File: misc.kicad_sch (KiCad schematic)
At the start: 35 parts

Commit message: [#54084] Sheets cleanup
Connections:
- net VDDI4 is gone; now on net VDDI: C?.1, C?.1, C?.1, C?.1, C?.1, C?.1, R?.2, R?.2, R?.2, R?.2, R?.2, R?.2, R?.2, R?.2, R?.2, R?.2, U?.C6 (VCCQ), U?.M4 (VCCQ), U?.N4 (VCCQ), U?.P3 (VCCQ), U?.P5 (VCCQ)
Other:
- note added: "PolarFire Bank 3 JTAG/DEDIO"
- note added: "PolarFire Bank 4 MSSIO"
- company: (none) -> Antmicro Ltd
- title: (none) -> PolarFire SoM
- moved on the sheet: C?, J?, R?, U?, U?D, U?E

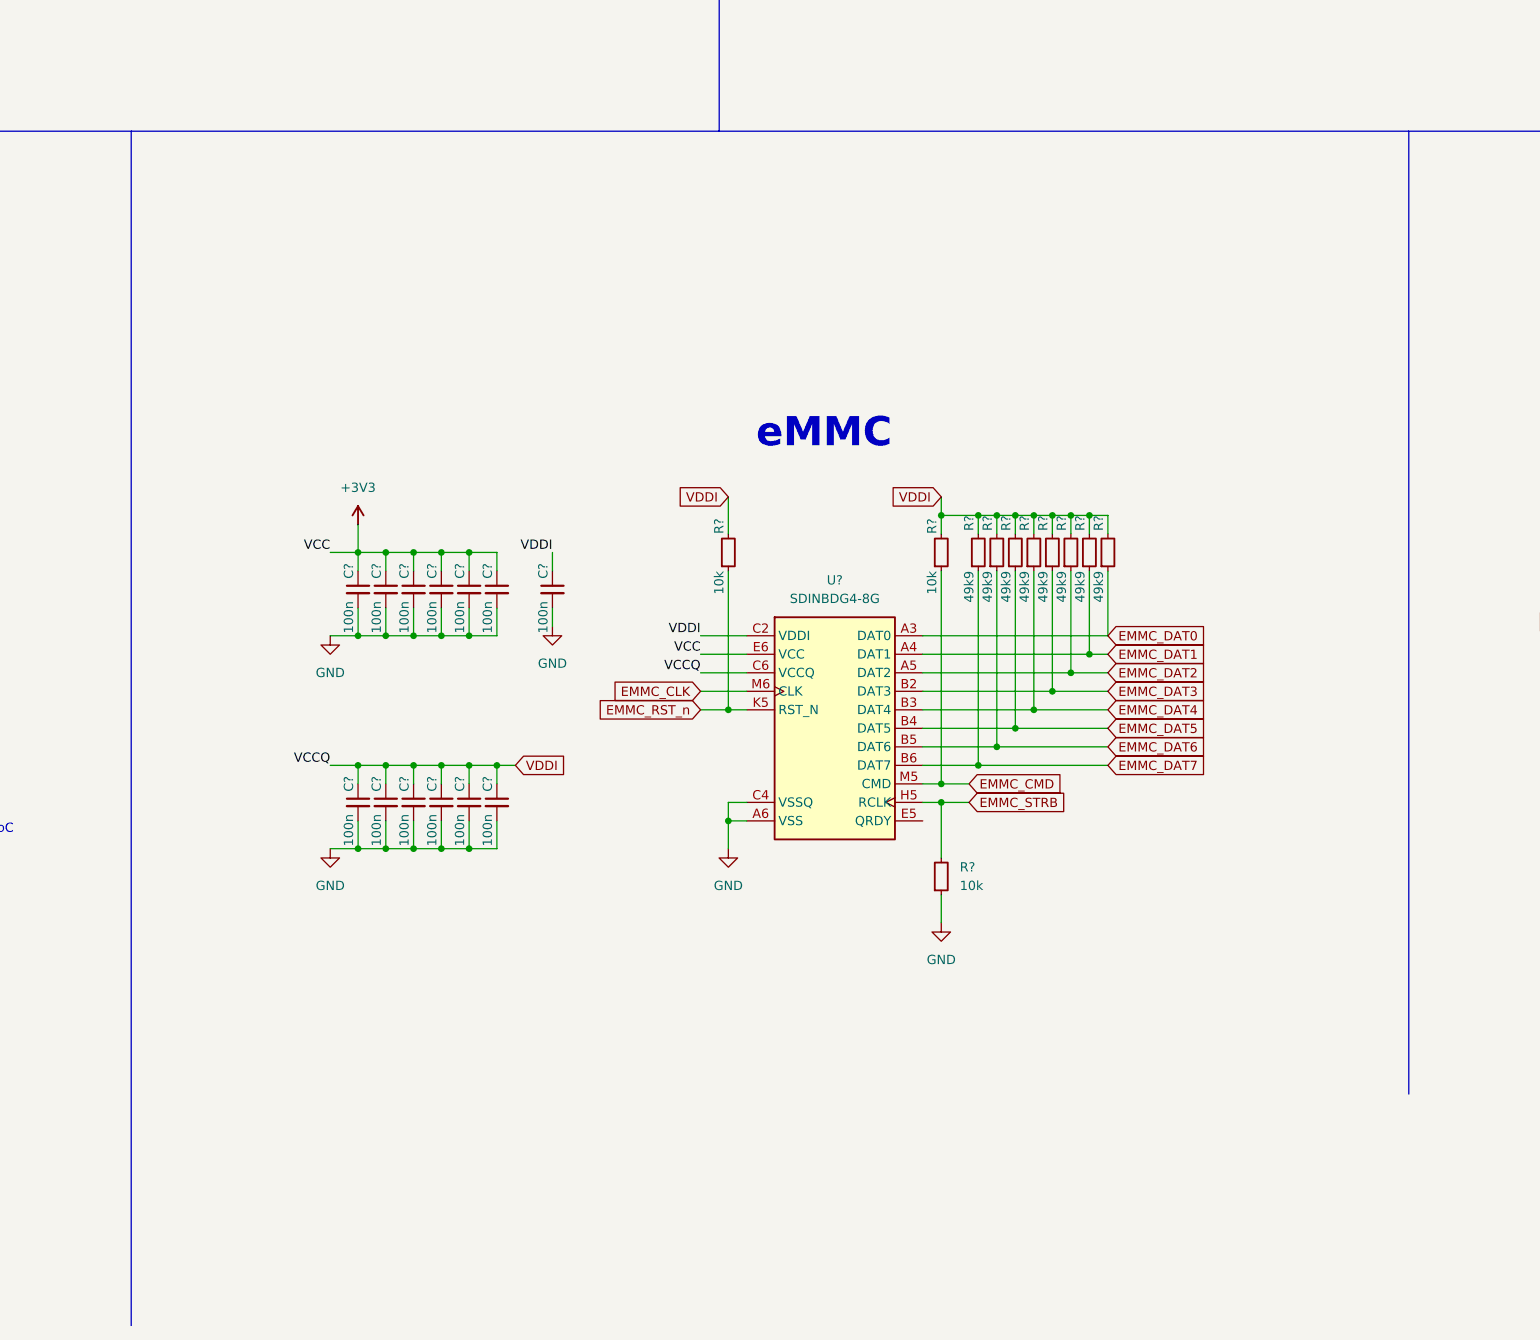
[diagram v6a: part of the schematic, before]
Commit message: [#54016] Relabel eMMC supply nets
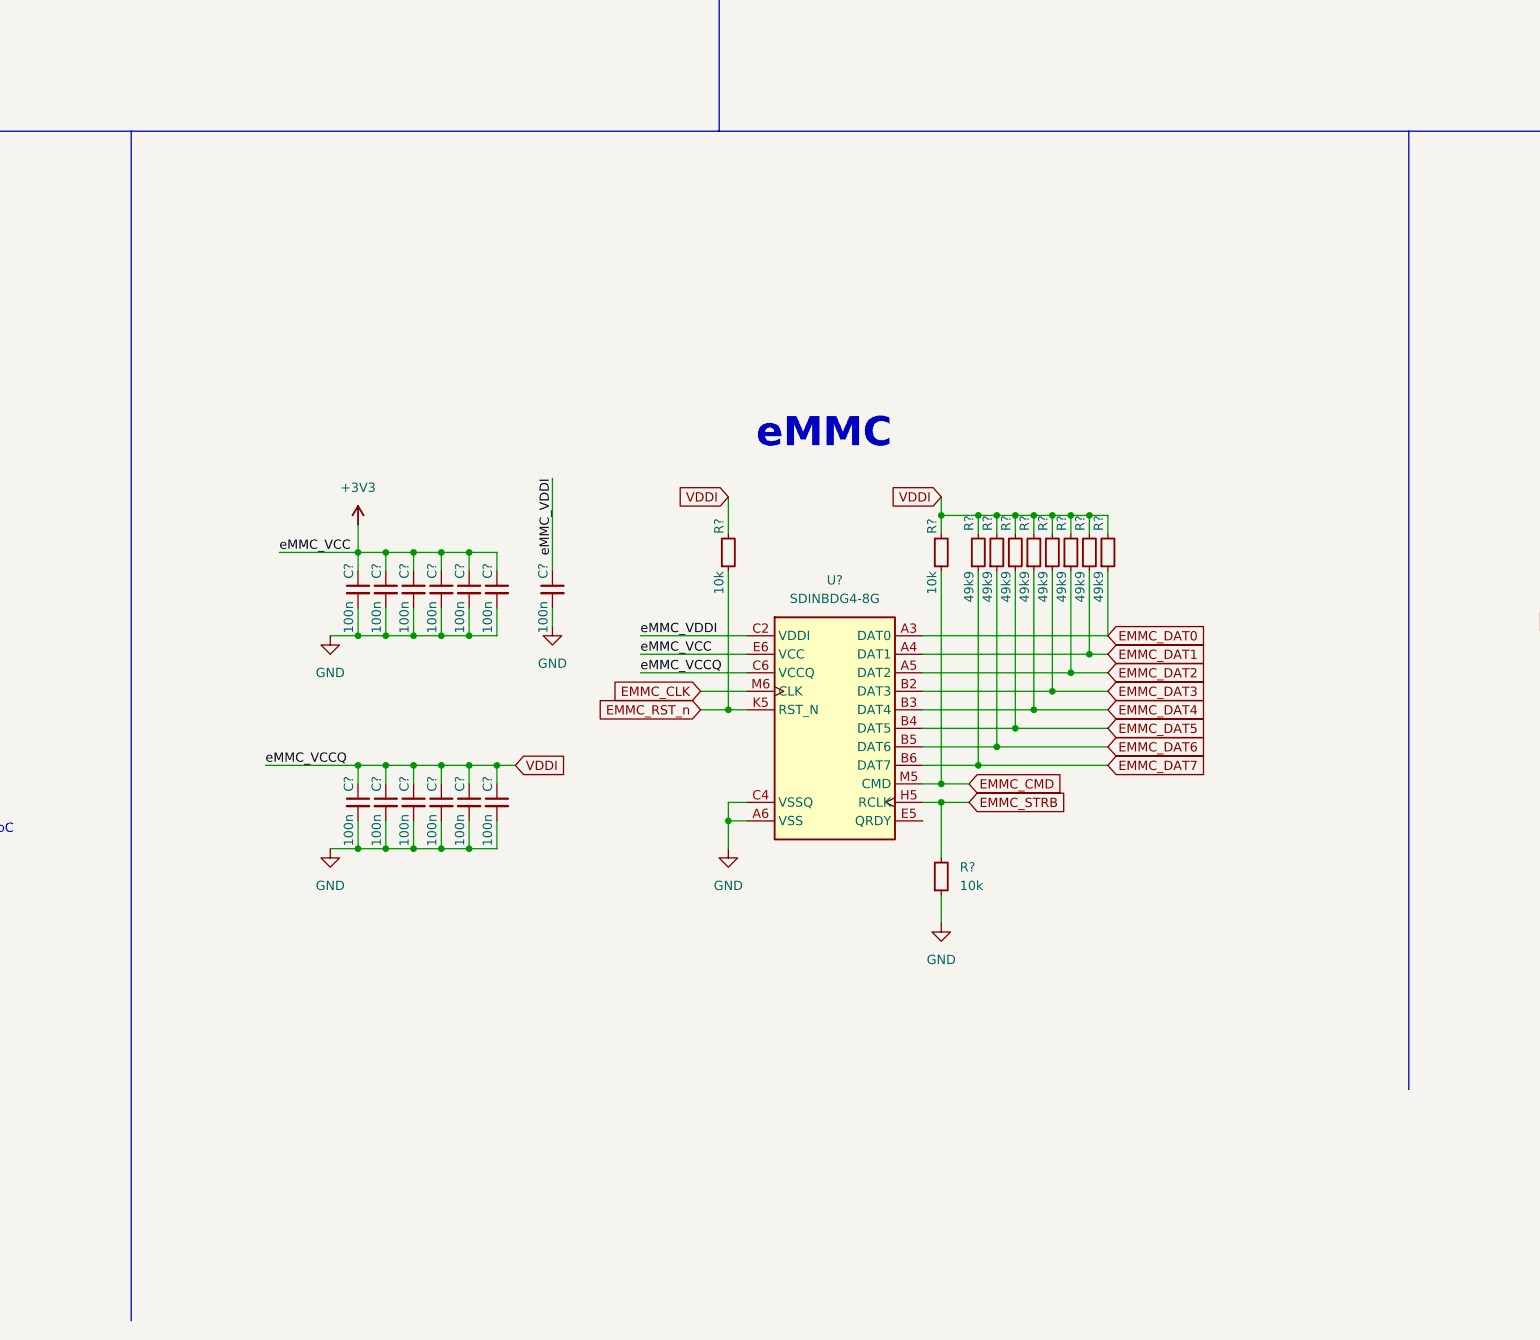
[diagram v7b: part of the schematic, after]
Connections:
- net VDDI: no longer C?.1, U?.C2 (VDDI)
- new net eMMC_VDDI: C?.1, U?.C2 (VDDI)
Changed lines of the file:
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@@
     (stroke (width 0) (type default) (color 0 0 0 0))
   )
-  (wire (pts (xy 165.1 179.07) (xy 168.91 179.07))
+  (wire (pts (xy 158.115 179.07) (xy 168.91 179.07))
     (stroke (width 0) (type default) (color 0 0 0 0))
   )
@@
     (stroke (width 0) (type default) (color 0 0 0 0))
   )
-  (polyline (pts (xy 137.795 285.115) (xy 137.795 121.285))
+  (polyline (pts (xy 137.795 284.48) (xy 137.795 121.285))
     (stroke (width 0) (type default) (color 0 0 0 0))
   )
@@
     (stroke (width 0) (type default) (color 0 0 0 0))
   )
-  (wire (pts (xy 165.1 208.28) (xy 168.91 208.28))
+  (wire (pts (xy 156.21 208.28) (xy 168.91 208.28))
     (stroke (width 0) (type default) (color 0 0 0 0))
   )
@@
     (stroke (width 0) (type default) (color 0 0 0 0))
   )
-  (wire (pts (xy 195.58 179.07) (xy 195.58 181.61))
+  (wire (pts (xy 195.58 168.91) (xy 195.58 181.61))
     (stroke (width 0) (type default) (color 0 0 0 0))
   )
@@
     (stroke (width 0) (type default) (color 0 0 0 0))
   )
-  (wire (pts (xy 215.9 195.58) (xy 222.25 195.58))
+  (wire (pts (xy 207.645 195.58) (xy 222.25 195.58))
     (stroke (width 0) (type default) (color 0 0 0 0))
   )
@@
     (stroke (width 0) (type default) (color 0 0 0 0))
   )
-  (wire (pts (xy 215.9 193.04) (xy 222.25 193.04))
+  (wire (pts (xy 207.645 193.04) (xy 222.25 193.04))
     (stroke (width 0) (type default) (color 0 0 0 0))
   )
@@
     (stroke (width 0) (type default) (color 0 0 0 0))
   )
-  (wire (pts (xy 215.9 190.5) (xy 222.25 190.5))
+  (wire (pts (xy 207.645 190.5) (xy 222.25 190.5))
     (stroke (width 0) (type default) (color 0 0 0 0))
   )
@@
     (stroke (width 0) (type default) (color 0 0 0 0))
   )
-  (polyline (pts (xy 313.055 253.365) (xy 313.055 121.285))
+  (polyline (pts (xy 313.055 252.73) (xy 313.055 121.285))
     (stroke (width 0) (type default) (color 0 0 0 0))
   )
@@
     (effects (font (size 4 4) (thickness 0.8) bold) (justify left bottom))
   )
-  (label "VCCQ" (at 215.9 195.58 180)
+  (label "eMMC_VCCQ" (at 207.645 195.58 0)
+    (effects (font (size 1.27 1.27)) (justify left bottom))
+  )
+  (label "eMMC_VCC" (at 158.115 179.07 0)
+    (effects (font (size 1.27 1.27)) (justify left bottom))
+  )
+  (label "eMMC_VCCQ" (at 156.21 208.28 0)
+    (effects (font (size 1.27 1.27)) (justify left bottom))
+  )
+  (label "eMMC_VCC" (at 207.645 193.04 0)
+    (effects (font (size 1.27 1.27)) (justify left bottom))
+  )
+  (label "eMMC_VDDI" (at 195.58 168.91 270)
     (effects (font (size 1.27 1.27)) (justify right bottom))
   )
-  (label "VCC" (at 165.1 179.07 180)
-    (effects (font (size 1.27 1.27)) (justify right bottom))
-  )
-  (label "VCCQ" (at 165.1 208.28 180)
-    (effects (font (size 1.27 1.27)) (justify right bottom))
-  )
-  (label "VCC" (at 215.9 193.04 180)
-    (effects (font (size 1.27 1.27)) (justify right bottom))
-  )
-  (label "VDDI" (at 195.58 179.07 180)
-    (effects (font (size 1.27 1.27)) (justify right bottom))
-  )
-  (label "VDDI" (at 215.9 190.5 180)
-    (effects (font (size 1.27 1.27)) (justify right bottom))
+  (label "eMMC_VDDI" (at 207.645 190.5 0)
+    (effects (font (size 1.27 1.27)) (justify left bottom))
   )
   (global_label "MEM_DAT4" (shape input) (at 85.725 77.47 0) (fields_autoplaced)

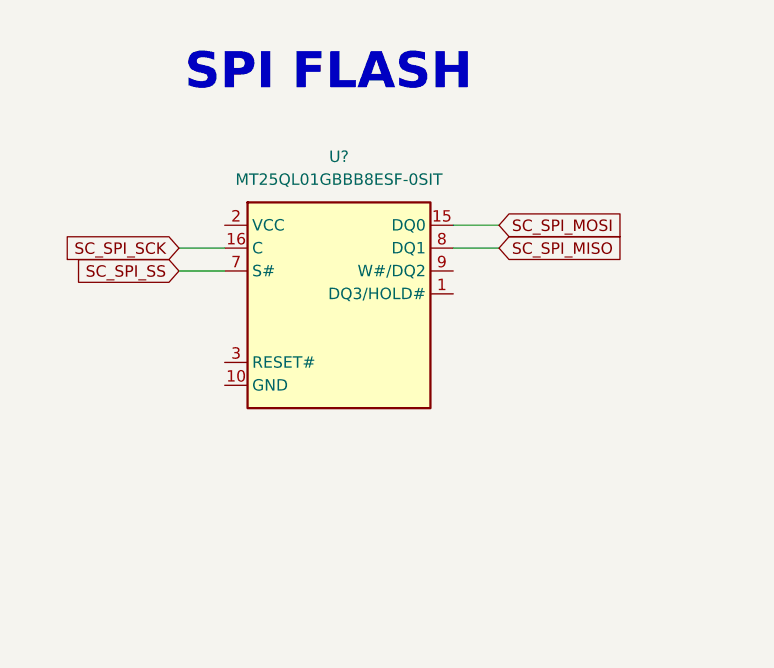
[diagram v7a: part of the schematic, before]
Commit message: [#54016] Connect power to SPI FLASH
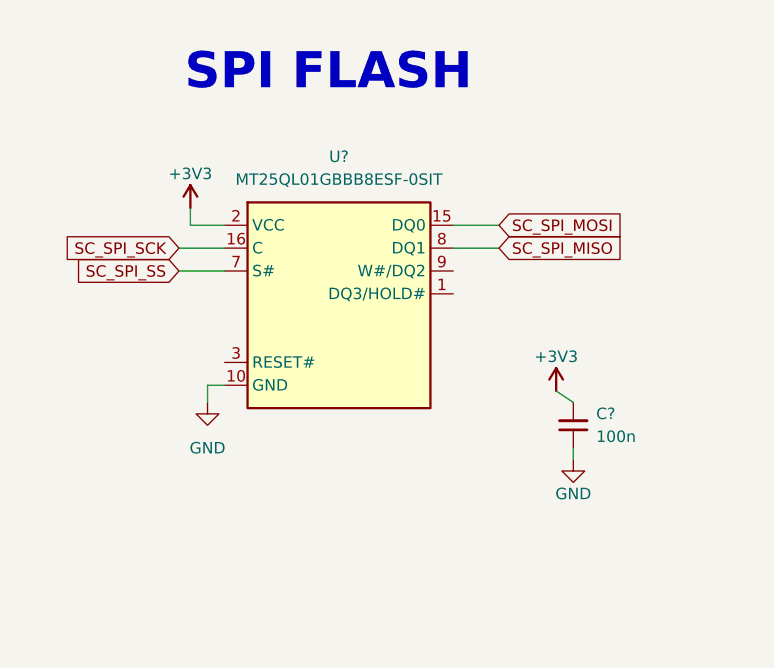
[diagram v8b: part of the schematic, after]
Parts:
- added C?: C_100n_0402, antmicro-footprints:C_0402_1005Metric, symbol antmicroCapacitors0402:C_100n_0402
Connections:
- net +3V3: now also U?.2 (VCC), C?.2
- net GND: now also U?.10 (GND), C?.1
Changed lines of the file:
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@@
     (stroke (width 0) (type default) (color 0 0 0 0))
   )
+  (wire (pts (xy 385.445 204.47) (xy 387.35 205.74))
+    (stroke (width 0) (type default) (color 0 0 0 0))
+  )
   (wire (pts (xy 184.15 215.9) (xy 184.15 219.71))
     (stroke (width 0) (type default) (color 0 0 0 0))
@@
     (stroke (width 0) (type default) (color 0 0 0 0))
   )
+  (wire (pts (xy 348.615 203.835) (xy 346.71 203.835))
+    (stroke (width 0) (type default) (color 0 0 0 0))
+  )
   (wire (pts (xy 264.16 173.99) (xy 266.7 173.99))
     (stroke (width 0) (type default) (color 0 0 0 0))
@@
     (stroke (width 0) (type default) (color 0 0 0 0))
   )
+  (wire (pts (xy 344.805 186.055) (xy 344.805 184.15))
+    (stroke (width 0) (type default) (color 0 0 0 0))
+  )
   (wire (pts (xy 259.08 173.99) (xy 261.62 173.99))
     (stroke (width 0) (type default) (color 0 0 0 0))
@@
     (stroke (width 0) (type default) (color 0 0 0 0))
   )
+  (wire (pts (xy 348.615 186.055) (xy 344.805 186.055))
+    (stroke (width 0) (type default) (color 0 0 0 0))
+  )
   (wire (pts (xy 256.54 173.99) (xy 259.08 173.99))
     (stroke (width 0) (type default) (color 0 0 0 0))
@@
     (stroke (width 0) (type default) (color 0 0 0 0))
   )
+  (wire (pts (xy 346.71 203.835) (xy 346.71 205.74))
+    (stroke (width 0) (type default) (color 0 0 0 0))
+  )
   (wire (pts (xy 133.35 68.58) (xy 138.43 68.58))
     (stroke (width 0) (type default) (color 0 0 0 0))
@@
     (stroke (width 0) (type default) (color 0 0 0 0))
   )
+  (wire (pts (xy 387.35 210.82) (xy 387.35 212.09))
+    (stroke (width 0) (type default) (color 0 0 0 0))
+  )
   (wire (pts (xy 67.945 69.85) (xy 73.025 69.85))
     (stroke (width 0) (type default) (color 0 0 0 0))
@@
     )
   )
+  (symbol (lib_id "antmicropower:+3V3") (at 385.445 204.47 0) (unit 1)
+    (in_bom yes) (on_board yes)
+    (property "Reference" "#PWR?" (id 0) (at 400.685 207.01 0)
+      (effects (font (size 1.27 1.27) (thickness 0.15)) (justify left bottom) hide)
+    )
+    (property "Value" "+3V3" (id 1) (at 385.445 200.66 0)
+      (effects (font (size 1.27 1.27) (thickness 0.15)))
+    )
+    (property "Footprint" "" (id 2) (at 400.685 212.09 0)
+      (effects (font (size 1.27 1.27) (thickness 0.15)) (justify left bottom) hide)
+    )
+    (property "Datasheet" "" (id 3) (at 400.685 214.63 0)
+      (effects (font (size 1.27 1.27) (thickness 0.15)) (justify left bottom) hide)
+    )
+    (property "Author" "Antmicro" (id 4) (at 400.685 212.09 0)
+      (effects (font (size 1.27 1.27) (thickness 0.15)) (justify left bottom) hide)
+    )
+    (property "License" "Apache-2.0" (id 5) (at 400.685 214.63 0)
+      (effects (font (size 1.27 1.27) (thickness 0.15)) (justify left bottom) hide)
+    )
+    (pin "1")
+  )
   (symbol (lib_id "antmicroResistors0402:R_49k9_0402") (at 256.54 181.61 90) (unit 1)
     (in_bom yes) (on_board yes)
@@
     (pin "1")
   )
+  (symbol (lib_id "antmicropower:GND") (at 346.71 205.74 0) (unit 1)
+    (in_bom yes) (on_board yes) (fields_autoplaced)
+    (property "Reference" "#PWR?" (id 0) (at 355.6 208.28 0)
+      (effects (font (size 1.27 1.27) (thickness 0.15)) (justify left bottom) hide)
+    )
+    (property "Value" "GND" (id 1) (at 346.71 210.82 0)
+      (effects (font (size 1.27 1.27) (thickness 0.15)))
+    )
+    (property "Footprint" "" (id 2) (at 355.6 213.36 0)
+      (effects (font (size 1.27 1.27) (thickness 0.15)) (justify left bottom) hide)
+    )
+    (property "Datasheet" "" (id 3) (at 355.6 218.44 0)
+      (effects (font (size 1.27 1.27) (thickness 0.15)) (justify left bottom) hide)
+    )
+    (property "Author" "Antmicro" (id 4) (at 355.6 213.36 0)
+      (effects (font (size 1.27 1.27) (thickness 0.15)) (justify left bottom) hide)
+    )
+    (property "License" "Apache-2.0" (id 5) (at 355.6 215.9 0)
+      (effects (font (size 1.27 1.27) (thickness 0.15)) (justify left bottom) hide)
+    )
+    (pin "1")
+  )
   (symbol (lib_id "antmicroMemory:MT25QL01GBBB8E_SOP2-16") (at 346.075 186.055 0) (unit 1)
     (in_bom yes) (on_board yes) (fields_autoplaced)
@@
     (pin "2")
   )
+  (symbol (lib_id "antmicropower:GND") (at 387.35 212.09 0) (unit 1)
+    (in_bom yes) (on_board yes)
+    (property "Reference" "#PWR?" (id 0) (at 396.24 214.63 0)
+      (effects (font (size 1.27 1.27) (thickness 0.15)) (justify left bottom) hide)
+    )
+    (property "Value" "GND" (id 1) (at 387.35 215.9 0)
+      (effects (font (size 1.27 1.27) (thickness 0.15)))
+    )
+    (property "Footprint" "" (id 2) (at 396.24 219.71 0)
+      (effects (font (size 1.27 1.27) (thickness 0.15)) (justify left bottom) hide)
+    )
+    (property "Datasheet" "" (id 3) (at 396.24 224.79 0)
+      (effects (font (size 1.27 1.27) (thickness 0.15)) (justify left bottom) hide)
+    )
+    (property "Author" "Antmicro" (id 4) (at 396.24 219.71 0)
+      (effects (font (size 1.27 1.27) (thickness 0.15)) (justify left bottom) hide)
+    )
+    (property "License" "Apache-2.0" (id 5) (at 396.24 222.25 0)
+      (effects (font (size 1.27 1.27) (thickness 0.15)) (justify left bottom) hide)
+    )
+    (pin "1")
+  )
   (symbol (lib_id "antmicroResistors0402:R_0R_0402") (at 75.565 96.52 0) (unit 1)
     (in_bom yes) (on_board yes)
@@
     (pin "2")
   )
+  (symbol (lib_id "antmicroCapacitors0402:C_100n_0402") (at 387.35 210.82 90) (unit 1)
+    (in_bom yes) (on_board yes) (fields_autoplaced)
+    (property "Reference" "C?" (id 0) (at 389.89 207.0035 90)
+      (effects (font (size 1.27 1.27) (thickness 0.15)) (justify right))
+    )
+    (property "Value" "C_100n_0402" (id 1) (at 397.51 190.5 0)
+      (effects (font (size 1.27 1.27) (thickness 0.15)) (justify left bottom) hide)
+    )
+    (property "Footprint" "antmicro-footprints:C_0402_1005Metric" (id 2) (at 400.05 190.5 0)
+      (effects (font (size 1.27 1.27) (thickness 0.15)) (justify left bottom) hide)
+    )
+    (property "Datasheet" "https://www.murata.com/products/productdetail?partno=GRM155R61H104KE14%23" (id 3) (at 402.59 190.5 0)
+      (effects (font (size 1.27 1.27) (thickness 0.15)) (justify left bottom) hide)
+    )
+    (property "MPN" "GRM155R61H104KE14D" (id 4) (at 405.13 190.5 0)
+      (effects (font (size 1.27 1.27) (thickness 0.15)) (justify left bottom) hide)
+    )
+    (property "Manufacturer" "Murata" (id 5) (at 407.67 190.5 0)
+      (effects (font (size 1.27 1.27) (thickness 0.15)) (justify left bottom) hide)
+    )
+    (property "License" "Apache-2.0" (id 6) (at 410.21 190.5 0)
+      (effects (font (size 1.27 1.27) (thickness 0.15)) (justify left bottom) hide)
+    )
+    (property "Author" "Antmicro" (id 7) (at 412.75 190.5 0)
+      (effects (font (size 1.27 1.27) (thickness 0.15)) (justify left bottom) hide)
+    )
+    (property "Val" "100n" (id 8) (at 389.89 209.5435 90)
+      (effects (font (size 1.27 1.27) (thickness 0.15)) (justify right))
+    )
+    (property "Voltage" "50V" (id 9) (at 415.29 190.5 0)
+      (effects (font (size 1.27 1.27)) (justify left bottom) hide)
+    )
+    (property "Dielectric" "X5R" (id 10) (at 417.83 190.5 0)
+      (effects (font (size 1.27 1.27)) (justify left bottom) hide)
+    )
+    (pin "1")
+    (pin "2")
+  )
   (symbol (lib_id "antmicroResistors0402:R_49k9_0402") (at 261.62 181.61 90) (unit 1)
     (in_bom yes) (on_board yes)
@@
     (pin "2")
   )
+  (symbol (lib_id "antmicropower:+3V3") (at 344.805 184.15 0) (unit 1)
+    (in_bom yes) (on_board yes)
+    (property "Reference" "#PWR?" (id 0) (at 360.045 186.69 0)
+      (effects (font (size 1.27 1.27) (thickness 0.15)) (justify left bottom) hide)
+    )
+    (property "Value" "+3V3" (id 1) (at 344.805 180.34 0)
+      (effects (font (size 1.27 1.27) (thickness 0.15)))
+    )
+    (property "Footprint" "" (id 2) (at 360.045 191.77 0)
+      (effects (font (size 1.27 1.27) (thickness 0.15)) (justify left bottom) hide)
+    )
+    (property "Datasheet" "" (id 3) (at 360.045 194.31 0)
+      (effects (font (size 1.27 1.27) (thickness 0.15)) (justify left bottom) hide)
+    )
+    (property "Author" "Antmicro" (id 4) (at 360.045 191.77 0)
+      (effects (font (size 1.27 1.27) (thickness 0.15)) (justify left bottom) hide)
+    )
+    (property "License" "Apache-2.0" (id 5) (at 360.045 194.31 0)
+      (effects (font (size 1.27 1.27) (thickness 0.15)) (justify left bottom) hide)
+    )
+    (pin "1")
+  )
   (symbol (lib_id "antmicroResistors0402:R_49k9_0402") (at 254 181.61 90) (unit 1)
